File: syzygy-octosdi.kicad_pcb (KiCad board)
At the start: 4 copper layers, 100 x 50 mm, 231 parts, among them CN1 QTH-020-01-F-D-DP-A, J1 Conn_BNC, J2 Conn_BNC, J3 Conn_BNC, J4 Conn_BNC, J5 Conn_BNC, J6 Conn_BNC, J7 Conn_BNC, J8 Conn_BNC, J9 Conn_02x03_Odd_Even, U1 LMH0344SQE_NOPB, U10 GS2988-INE3, U11 STM32G031G8Ux, U2 LMH0344SQE_NOPB, U3 LMH0344SQE_NOPB, U4 LMH0344SQE_NOPB, U5 PCAL6416AHF, U6 PCAL6416AHF, U7 GS2988-INE3, U8 GS2988-INE3, U9 GS2988-INE3, X1 SX7DF148_500B20F30DNN

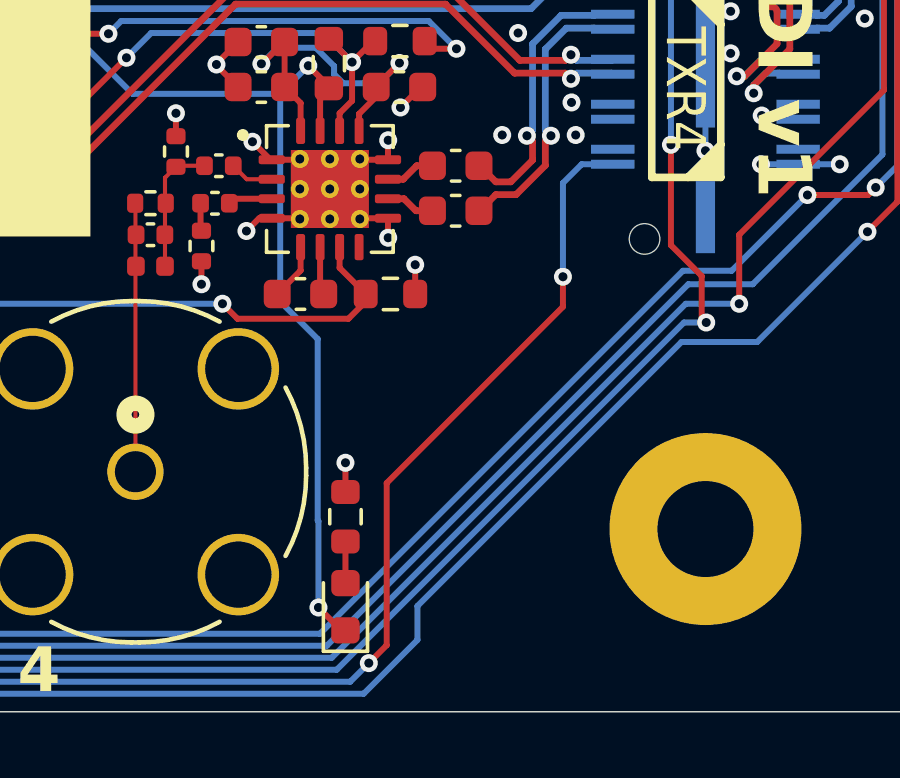
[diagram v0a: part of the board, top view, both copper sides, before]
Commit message: add some larger bypass caps to the cable drivers
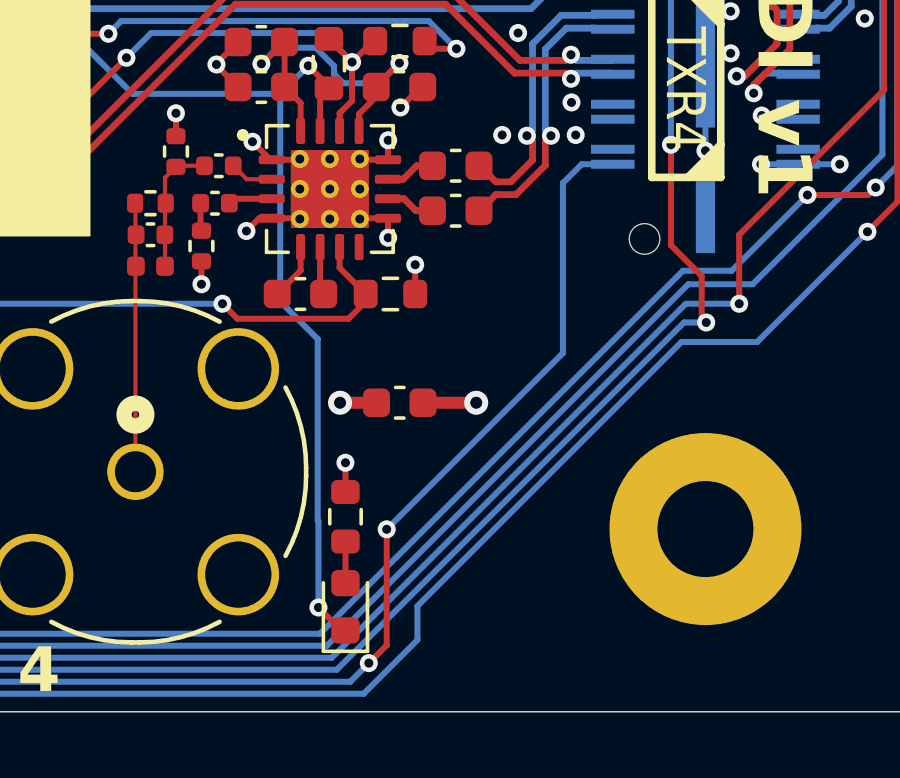
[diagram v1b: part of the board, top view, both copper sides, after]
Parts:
- added C3: 4u7, Capacitor_SMD:C_0603_1608Metric, F.Cu at (132.8, 89.7)
- renumbered C9 to C10, C10 to C11, C11 to C12, C12 to C13, C13 to C14, C14 to C15, C15 to C16, C16 to C17, C17 to C18, C18 to C19, C19 to C20, C20 to C21, C21 to C22, C22 to C23, C23 to C24, C24 to C25, C25 to C26, C26 to C27, C27 to C28, C28 to C29, C29 to C30, C30 to C31, C31 to C32, C32 to C33, C33 to C34, C34 to C35, C35 to C36, C36 to C37, C37 to C38, C38 to C39, C3 to C4, C39 to C40, C40 to C41, C41 to C42, C42 to C43, C43 to C44, C44 to C45, C45 to C46, C46 to C47, C47 to C48, C48 to C49, C4 to C5, C49 to C50, C50 to C51, C51 to C52, C52 to C53, C53 to C54, C54 to C55, C55 to C56, C56 to C57, C57 to C58, C58 to C59, C5 to C6, C59 to C60, C60 to C61, C61 to C62, C62 to C63, C63 to C64, C64 to C65, C65 to C66, C66 to C67, C67 to C68, C68 to C69, C6 to C7, C69 to C70, C70 to C71, C71 to C72, C72 to C73, C73 to C74, C74 to C75, C75 to C76, C76 to C77, C77 to C78, C78 to C79, C7 to C8, C79 to C80, C80 to C81, C81 to C82, C82 to C83, C83 to C84, C84 to C85, C85 to C86, C86 to C87, C8 to C9
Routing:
- net +3V3: track 709.3 -> 713.4 mm, vias 47 -> 48
- net GND: track 144.8 -> 146.1 mm, vias 92 -> 93

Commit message: specify led colours
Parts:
- D1: value LED -> LED Red
- D10, D11, D2, D3, D4, D5, D6, D7, D8, D9: value LED -> LED Green
- D12: value LED -> LED Orange
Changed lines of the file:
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@@
 			)
 		)
-		(property "Value" "LED"
+		(property "Value" "LED Green"
 			(at 0 1.43 0)
 			(layer "F.Fab")
@@
 			)
 		)
-		(property "Value" "LED"
+		(property "Value" "LED Green"
 			(at 0 1.43 90)
 			(layer "F.Fab")
@@
 			)
 		)
-		(property "Value" "LED"
+		(property "Value" "LED Green"
 			(at 0 1.43 90)
 			(layer "F.Fab")
@@
 			)
 		)
-		(property "Value" "LED"
+		(property "Value" "LED Green"
 			(at 0 1.43 90)
 			(layer "F.Fab")
@@
 			)
 		)
-		(property "Value" "LED"
+		(property "Value" "LED Green"
 			(at 0 1.43 90)
 			(layer "F.Fab")
@@
 			)
 		)
-		(property "Value" "LED"
+		(property "Value" "LED Green"
 			(at 0 1.43 90)
 			(layer "F.Fab")
@@
 			)
 		)
-		(property "Value" "LED"
+		(property "Value" "LED Orange"
 			(at 0 1.43 0)
 			(layer "F.Fab")
@@
 			)
 		)
-		(property "Value" "LED"
+		(property "Value" "LED Red"
 			(at 0 1.43 0)
 			(layer "F.Fab")
@@
 			)
 		)
-		(property "Value" "LED"
+		(property "Value" "LED Green"
 			(at 0 1.43 0)
 			(layer "F.Fab")
@@
 			)
 		)
-		(property "Value" "LED"
+		(property "Value" "LED Green"
 			(at 0 1.43 90)
 			(layer "F.Fab")
@@
 			)
 		)
-		(property "Value" "LED"
+		(property "Value" "LED Green"
 			(at 0 1.43 90)
 			(layer "F.Fab")
@@
 			)
 		)
-		(property "Value" "LED"
+		(property "Value" "LED Green"
 			(at 0 1.43 90)
 			(layer "F.Fab")

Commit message: add vio test point
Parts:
- added TP6: TestPoint, TestPoint:TestPoint_Pad_D1.0mm, F.Cu at (135.4, 87.9)
- renumbered TP9 to TP10, TP10 to TP11, TP11 to TP12, TP12 to TP13, TP13 to TP14, TP14 to TP15, TP6 to TP7, TP7 to TP8, TP8 to TP9
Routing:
- net /VIO: track 152.1 -> 154.5 mm, vias 11 -> 12
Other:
- board text added: "VIO"
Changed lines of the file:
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@@
 		(descr "SMD pad as test Point, diameter 1.0mm")
 		(tags "test point SMD pad")
-		(property "Reference" "TP12"
+		(property "Reference" "TP13"
 			(at 0 -1.448 0)
 			(layer "F.SilkS")
@@
 		(descr "SMD pad as test Point, diameter 1.0mm")
 		(tags "test point SMD pad")
-		(property "Reference" "TP7"
+		(property "Reference" "TP8"
 			(at 0 -1.448 0)
 			(layer "F.SilkS")
@@
 		(descr "SMD pad as test Point, diameter 1.0mm")
 		(tags "test point SMD pad")
-		(property "Reference" "TP9"
+		(property "Reference" "TP10"
 			(at 0 -1.448 0)
 			(layer "F.SilkS")
@@
 		(descr "SMD pad as test Point, diameter 1.0mm")
 		(tags "test point SMD pad")
-		(property "Reference" "TP11"
+		(property "Reference" "TP12"
 			(at 0 -1.448 0)
 			(layer "F.SilkS")
@@
 		(descr "SMD pad as test Point, diameter 1.0mm")
 		(tags "test point SMD pad")
-		(property "Reference" "TP10"
+		(property "Reference" "TP11"
 			(at 0 -1.448 0)
 			(layer "F.SilkS")
@@
 		(descr "SMD pad as test Point, diameter 1.0mm")
 		(tags "test point SMD pad")
-		(property "Reference" "TP13"
+		(property "Reference" "TP14"
 			(at 2.4 0 0)
 			(layer "F.SilkS")
@@
 		(descr "SMD pad as test Point, diameter 1.0mm")
 		(tags "test point SMD pad")
-		(property "Reference" "TP8"
+		(property "Reference" "TP9"
 			(at 0 -1.448 0)
 			(layer "F.SilkS")
@@
 		(descr "SMD pad as test Point, diameter 1.0mm")
 		(tags "test point SMD pad")
-		(property "Reference" "TP14"
+		(property "Reference" "TP15"
 			(at 2.3 0 0)
 			(layer "F.SilkS")
@@
 		(descr "SMD pad as test Point, diameter 1.0mm")
 		(tags "test point SMD pad")
-		(property "Reference" "TP6"
+		(property "Reference" "TP7"
 			(at 0 -1.448 0)
 			(layer "F.SilkS")
@@
 		)
 	)
+	(footprint "TestPoint:TestPoint_Pad_D1.0mm"
+		(layer "F.Cu")
+		(at 135.36 87.9)
+		(descr "SMD pad as test Point, diameter 1.0mm")
+		(tags "test point SMD pad")
+		(property "Reference" "TP6"
+			(at 0 -1.448 0)
+			(layer "F.SilkS")
+			(hide yes)
+			(effects
+				(font
+					(size 1 1)
+					(thickness 0.15)
+				)
+			)
+		)
+		(property "Value" "TestPoint"
+			(at 0 1.55 0)
+			(layer "F.Fab")
+			(effects
+				(font
+					(size 1 1)
+					(thickness 0.15)
+				)
+			)
+		)
+		(property "Datasheet" ""
+			(at 0 0 0)
+			(unlocked yes)
+			(layer "F.Fab")
+			(hide yes)
+			(effects
+				(font
+					(size 1.27 1.27)
+					(thickness 0.15)
+				)
+			)
+		)
+		(property "Description" "test point"
+			(at 0 0 0)
+			(unlocked yes)
+			(layer "F.Fab")
+			(hide yes)
+			(effects
+				(font
+					(size 1.27 1.27)
+					(thickness 0.15)
+				)
+			)
+		)
+		(property ki_fp_filters "Pin* Test*")
+		(sheetname "/")
+		(sheetfile "syzygy-octosdi.kicad_sch")
+		(units
+			(unit
+				(name "A")
+				(pins "1")
+			)
+		)
+		(attr exclude_from_bom)
+		(duplicate_pad_numbers_are_jumpers no)
+		(fp_circle
+			(center 0 0)
+			(end 0 0.7)
+			(stroke
+				(width 0.12)
+				(type solid)
+			)
+			(fill no)
+			(layer "F.SilkS")
+		)
+		(fp_circle
+			(center 0 0)
+			(end 1 0)
+			(stroke
+				(width 0.05)
+				(type solid)
+			)
+			(fill no)
+			(layer "F.CrtYd")
+		)
+		(fp_text user "${REFERENCE}"
+			(at 0 -1.45 0)
+			(layer "F.Fab")
+			(effects
+				(font
+					(size 1 1)
+					(thickness 0.15)
+				)
+			)
+		)
+		(pad "1" smd circle
+			(at 0 0)
+			(size 1 1)
+			(layers "F.Cu" "F.Mask")
+			(net "/VIO")
+			(pinfunction "1_1")
+			(pintype "passive")
+		)
+		(embedded_fonts no)
+	)
 	(footprint "JLCImport:QTH-020-01-F-D-DP-A"
 		(layer "B.Cu")
@@
 		)
 	)
+	(gr_text "VIO"
+		(at 136.54 88.5 0)
+		(layer "F.SilkS")
+		(effects
+			(font
+				(size 1 1)
+				(thickness 0.15)
+			)
+			(justify left bottom)
+		)
+	)
 	(gr_text "SWD"
 		(at 50.92 84.01 0)
@@
 	)
 	(segment
+		(start 135.36 87.9)
+		(end 136.44 87.9)
+		(width 0.2)
+		(layer "F.Cu")
+		(net "/VIO")
+	)
+	(segment
 		(start 97.005 64.58)
 		(end 96.575 64.15)
@@
 	)
 	(segment
+		(start 136.44 87.9)
+		(end 137.4175 88.8775)
+		(width 0.2)
+		(layer "F.Cu")
+		(net "/VIO")
+	)
+	(segment
 		(start 98.15 77.37)
 		(end 98.15 78.5625)
@@
 	)
 	(via
+		(at 137.4175 88.8775)
+		(size 0.6)
+		(drill 0.3)
+		(layers "F.Cu" "B.Cu")
+		(net "/VIO")
+	)
+	(via
 		(at 132.375 93.92)
 		(size 0.6)
@@
 	)
 	(segment
+		(start 137.4175 88.8775)
+		(end 138.25 88.045)
+		(width 0.2)
+		(layer "B.Cu")
+		(net "/VIO")
+	)
+	(segment
 		(start 72.4 78.5)
 		(end 72.1 78.2)
@@
 	(segment
 		(start 132.375 93.92)
-		(end 138.25 88.045)
+		(end 137.4175 88.8775)
 		(width 0.2)
 		(layer "B.Cu")

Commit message: sku and led resistor updates following review
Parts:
- R78, R79: value 4k7 -> 2k2
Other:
- board text added: "POD-OCTOSDI Rev1"
- board text removed: "POD-OCTOSDI v1"
